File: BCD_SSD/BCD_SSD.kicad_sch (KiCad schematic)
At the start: 40 parts, among them J1 Conn_01x06, J2 Conn_01x07, U1 Inverter, U10 AND-3, U11 AND-3, U12 AND-3, U13 AND-3, U14 AND-4, U15 OR, U16 OR-3, U17 OR, U18 AND, U19 AND, U2 Inverter, U20 AND-3, U21 OR, U22 OR-3, U23 AND-4, U24 AND-3, U25 OR, U26 AND-3, U27 AND-3, U28 OR, U29 AND, U3 Inverter, U30 AND-3, U31 OR-3, U32 AND-3, U33 AND, U34 AND-3, U35 OR-3, U36 AND-3, U37 OR, U38 AND-3, U4 Inverter, U5 AND-4, U6 AND-3, U7 OR, U8 AND-3, U9 AND-3

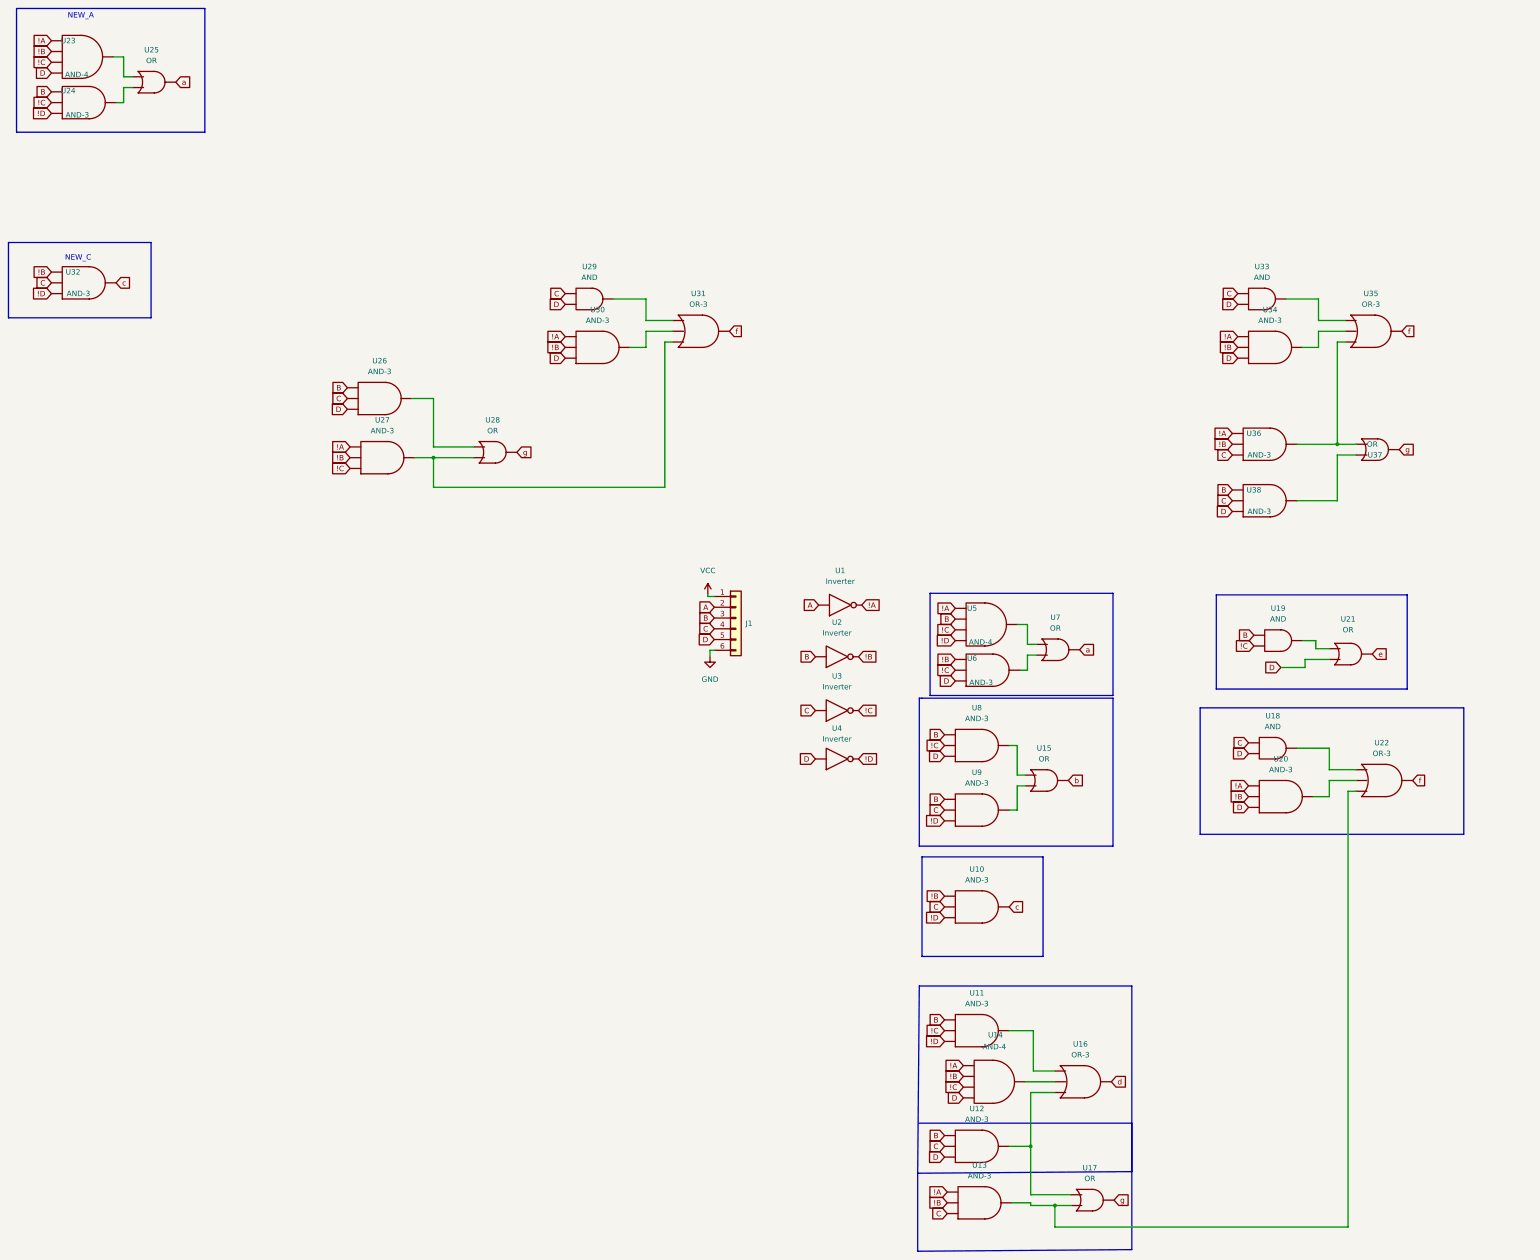
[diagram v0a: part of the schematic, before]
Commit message: Updated schematic to be correct. Added gitignore. Removed lock files
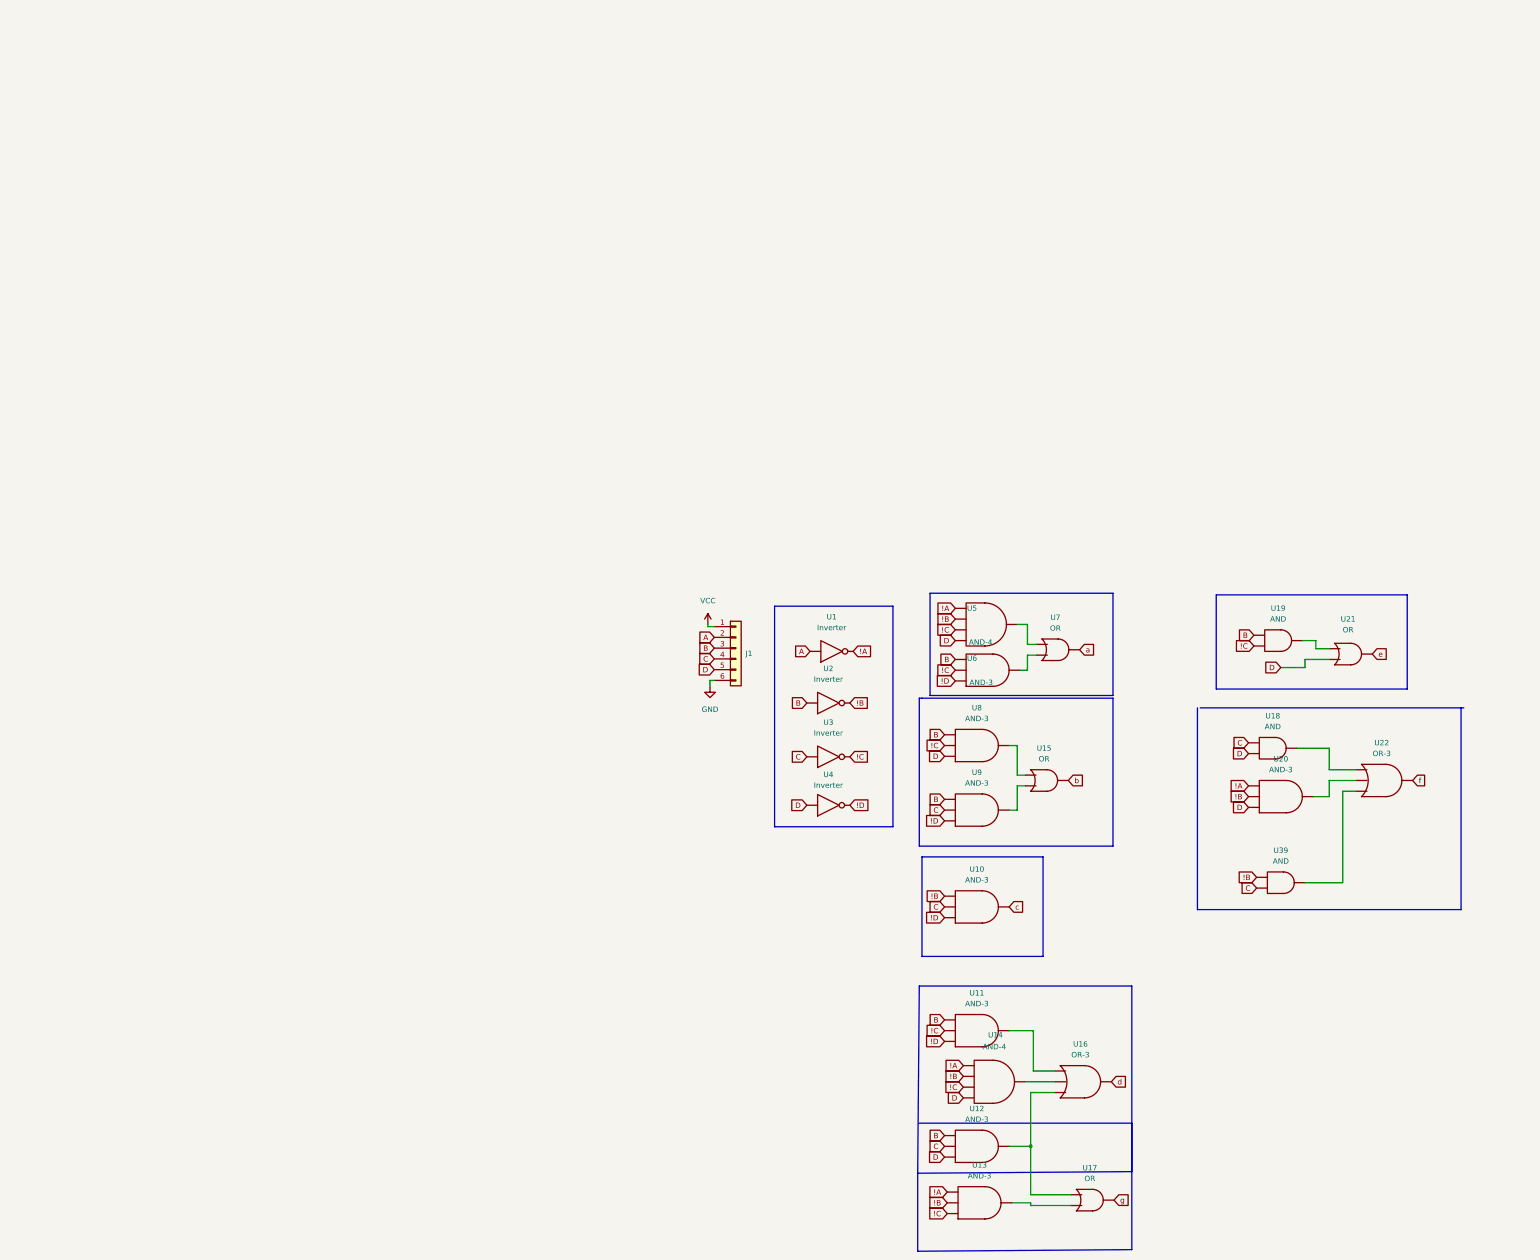
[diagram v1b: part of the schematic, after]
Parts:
- removed U23: AND-4, symbol AOI_Symbols:AND-4
- removed U24, U26, U27, U30, U32, U34, U36, U38: AND-3, symbol AOI_Symbols:AND-3
- removed U25, U28, U37: OR, symbol AOI_Symbols:OR
- removed U29, U33: AND, symbol AOI_Symbols:AND
- removed U31, U35: OR-3, symbol AOI_Symbols:OR-3
- added U39: AND, symbol AOI_Symbols:AND
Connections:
- net !B: now also U5., U39.; no longer U6.
- net !C: now also U13.
- net !D: now also U6.; no longer U5.
- net B: now also U6.; no longer U5.
- net C: now also U39.; no longer U13.
- net D: now also U5.; no longer U6.
- new net: U15., U9.
- new net: U15., U8.
- new net: U11., U16.
- new net: U12., U16., U17.
- new net: U13., U17.
- new net: U19., U21.
- new net: U14., U16.
- new net: U6., U7.
- new net: U5., U7.
- new net: U18., U22.
- new net: U20., U22.
- new net: U22., U39.
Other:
- note removed: "NEW_A"
- note removed: "NEW_C"
- moved on the sheet: J1, U1, U2, U3, U4

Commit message: Theoretically correct decoder
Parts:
- removed U11: AND-3, symbol AOI_Symbols:AND-3
- removed U14: AND-4, symbol AOI_Symbols:AND-4
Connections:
- net ~{ABC}D: now reaches U16.
- net ~{ABC}D: now also U5., U7.
- net B~{CD}: now reaches U6., U7.
- net B~{CD}: now also U16.
- new net: U15., U9.
- new net: U15., U8.
- new net: U12., U16., U17.
- new net: U13., U17.
- new net: U19., U21.
- new net: U18., U22.
- new net: U20., U22.
- new net: U22., U39.
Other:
- moved on the sheet: U7
